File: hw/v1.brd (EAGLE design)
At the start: 32 x 37 mm, 43 parts, among them J1 FFC2B28-24-G, J2 S2B-PH-SM4-TB(LF)(SN), J3 10118193-0001LF, Q1 SI1308EDL-T1-GE3, SW1 SMD-BUTTON(4P-5.2X5.2X1.5MM-S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, U1 ESP32-C3-WROOM-02-H4, U2 PCF85063ATT/AJ, U3 TLV1117LV33DCYR

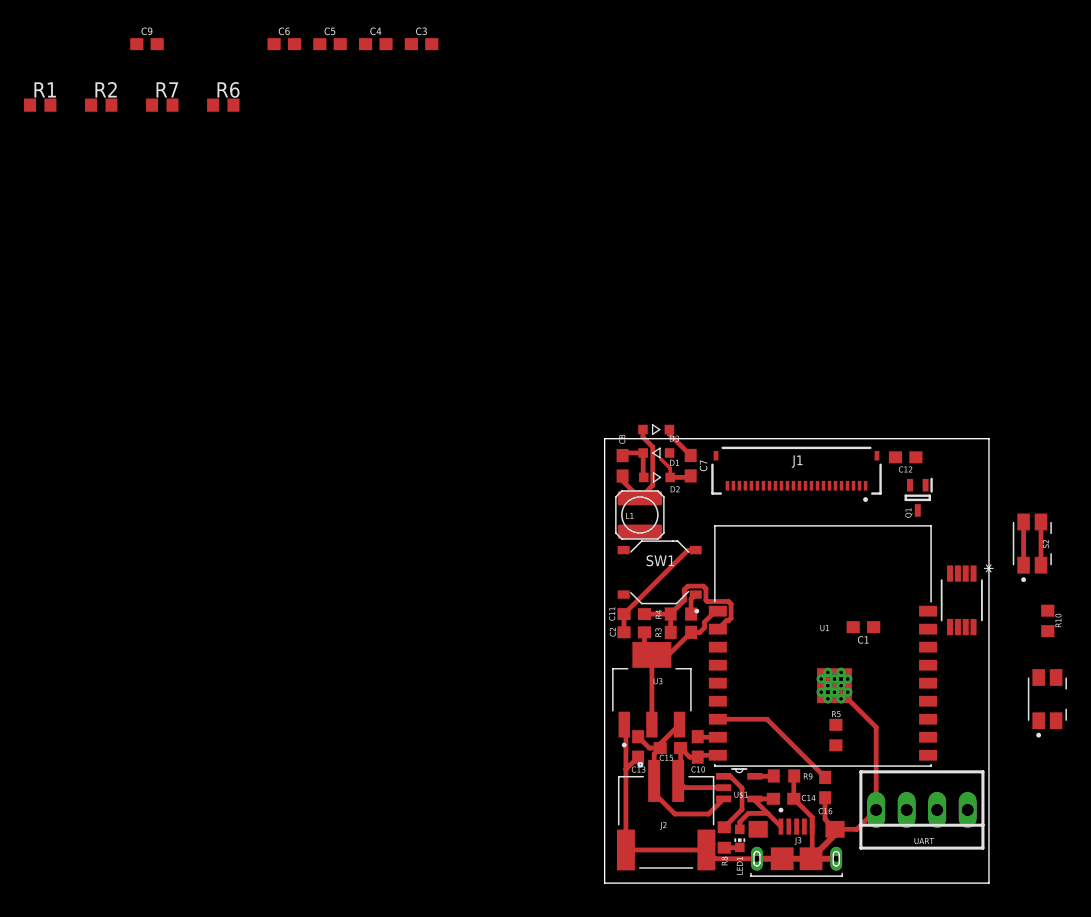
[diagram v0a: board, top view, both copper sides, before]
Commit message: Finish basic board layout, change reset button
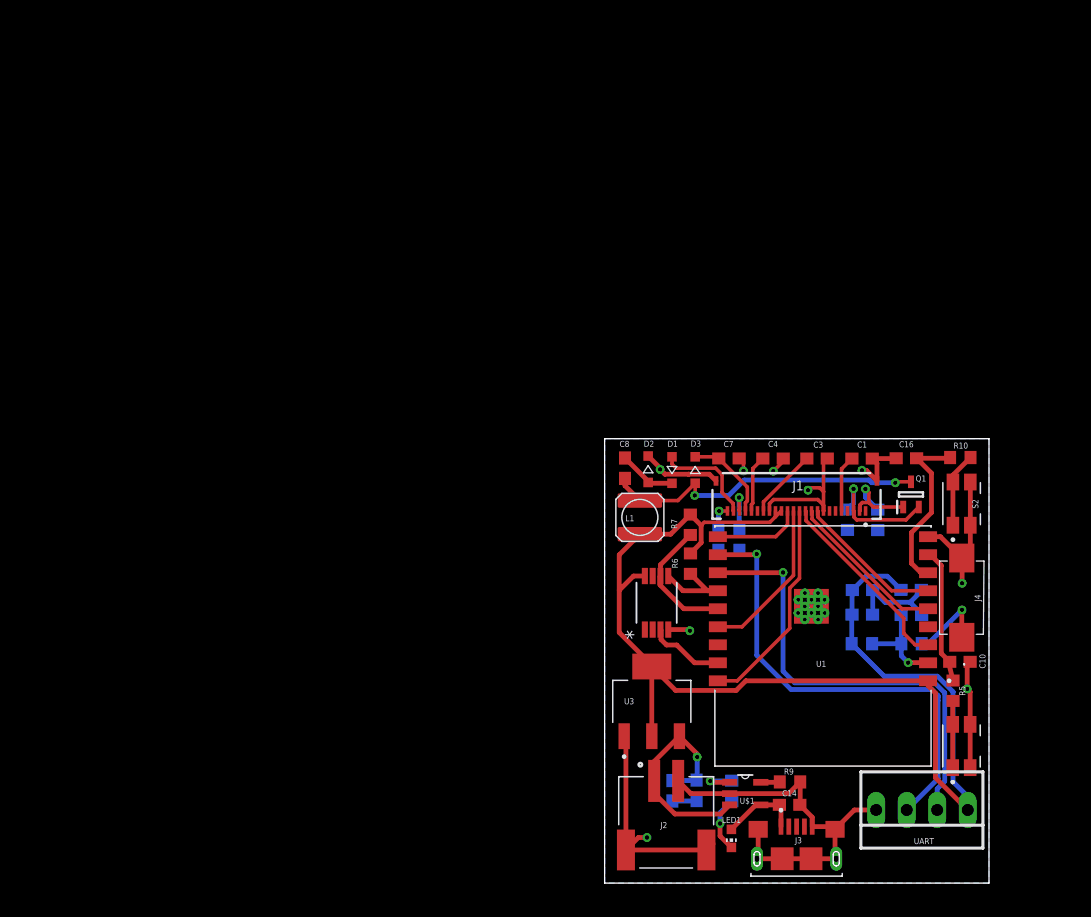
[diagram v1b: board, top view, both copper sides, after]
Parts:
- removed SW1: SMD-BUTTON(4P-5.2X5.2X1.5MM-SKQGADE010)-SKQGADE010, SMD-BUTTON_4P-5.2X5.2X1.5MM-SKQGADE010_:SW4-SMD-5.2X5.2X1.5MM
- added J4: PTS636_SM25F_SMTR_LFS, PTS636_SM25F_SMTR_LFS:PTS636SM25FSMTRLFS
- moved C9 78.2 mm to (25.5, 24.4), flipped to the bottom, turned to 180 degrees
- moved R1 77.8 mm to (22.7, 30.2), flipped to the bottom, turned to 90 degrees
- moved R2 71.1 mm to (20.2, 30.3), flipped to the bottom, turned to 90 degrees
- moved R7 56.2 mm to (7.13, 29.8), turned to 90 degrees
- moved C6 54.9 mm to (9.48, 28.6), flipped to the bottom, turned to 270 degrees
- moved R6 54.5 mm to (7.15, 26.6), turned to 90 degrees
- moved C5 53.5 mm to (11.2, 28.6), flipped to the bottom, turned to 270 degrees
- moved C4 47.8 mm to (14.0, 35.4)
- moved C3 47.7 mm to (17.7, 35.3)
- moved C16 28.2 mm to (25.1, 35.4), turned to 180 degrees
- moved U2 25.4 mm to (4.33, 23.3), turned to 90 degrees
- moved C11 23.1 mm to (25.5, 22.3), flipped to the bottom
- moved C10 23.0 mm to (29.6, 18.4), turned to 0 degrees
- moved R4 19.4 mm to (25.6, 19.9), flipped to the bottom, turned to 0 degrees
- moved C2 19.0 mm to (21.5, 22.3), flipped to the bottom
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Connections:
- net BUSY: now also U1.6; no longer U1.3
- net CS: now also U1.18; no longer U1.10
- net D/C: now also U1.3; no longer U1.15
- net GND: now also J4.2; no longer SW1.3
- net MOSI: now also U1.10; no longer U1.6
- net N$8: now also J4.1; no longer SW1.1
- net RES: now also U1.5; no longer U1.18
- net SCK: now also U1.15; no longer U1.5
- net SCL: now also R7.1, U1.14; no longer R6.1, U1.13
- net SDA: now also R6.1, U1.13; no longer R7.1, U1.14
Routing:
- net 3V3: track 15.4 -> 104.0 mm
- net N$12: track 0.00 -> 38.8 mm, vias 0 -> 1
- net GND: track 89.8 -> 127.8 mm, vias 0 -> 9
- net N$11: track 0.00 -> 37.9 mm, vias 0 -> 1
- net N$5: track 8.94 -> 27.3 mm, vias 0 -> 2
- net CS: track 0.00 -> 17.9 mm
- net D/C: track 0.00 -> 16.0 mm
- net RES: track 0.00 -> 13.4 mm
- net SCK: track 0.00 -> 13.4 mm
- net BUSY: track 0.00 -> 12.2 mm
- net SCL: track 0.00 -> 10.8 mm
- net RESE: track 0.00 -> 10.2 mm, vias 0 -> 1
- net BTN2: track 2.20 -> 11.4 mm
- net PREVGL: track 0.00 -> 8.55 mm
- net GDR: track 0.00 -> 7.76 mm, vias 0 -> 1
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- added copper zone on layer 16, net GND
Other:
- board text added: "Ian Feldman 2024"

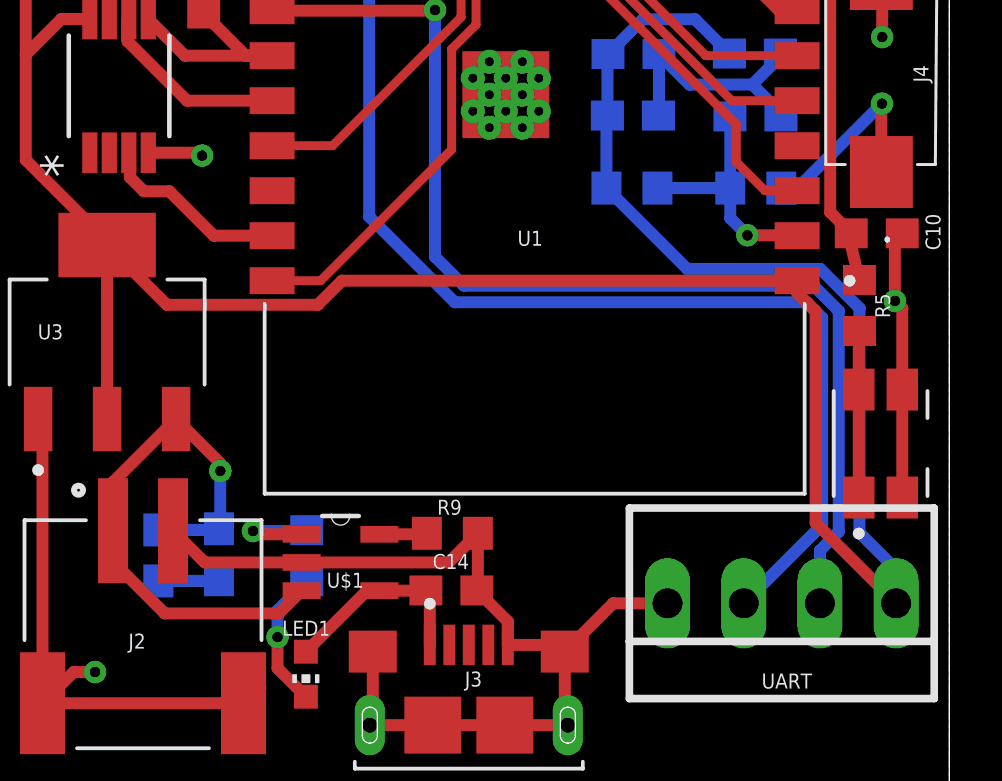
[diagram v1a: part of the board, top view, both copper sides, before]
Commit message: Add temperature sensor
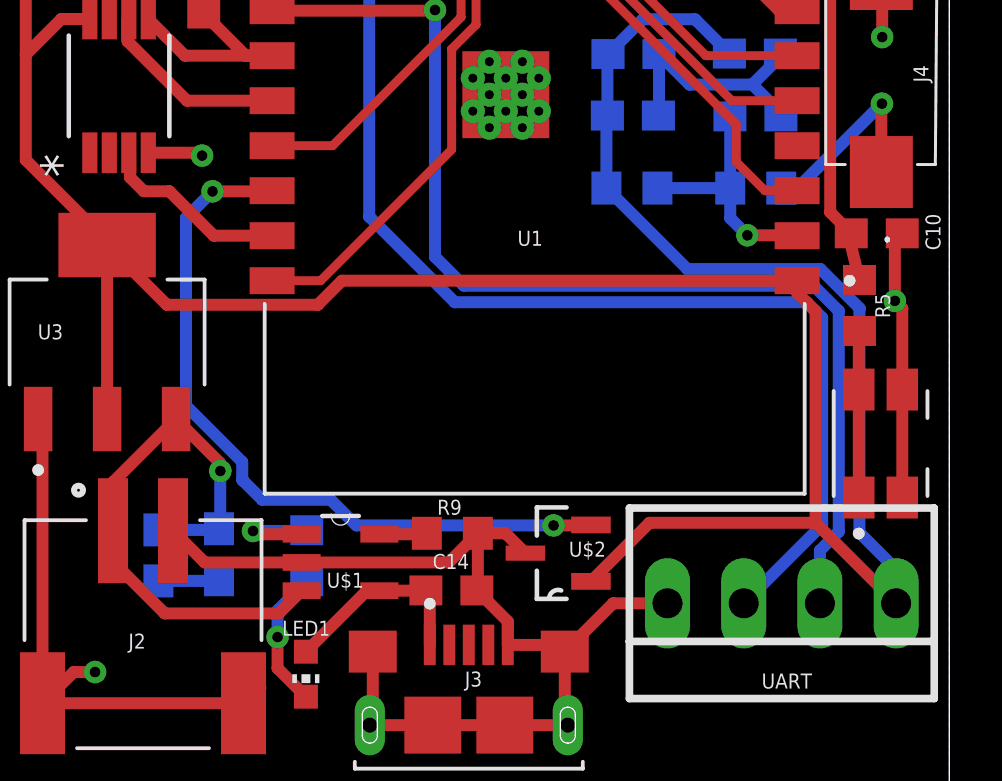
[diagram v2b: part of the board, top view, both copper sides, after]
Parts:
- added U$2: MCP9700T-E/TT, MCP9700T-E_TT:SOT95P237X112-3N
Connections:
- new net TEMP: U$2.2, U1.16
- net 3V3: now also U$2.1
- net GND: now also U$2.3
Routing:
- net TEMP: track 0.00 -> 25.0 mm, vias 0 -> 2
- net 3V3: track 104.0 -> 112.3 mm
- net GND: track 127.8 -> 129.7 mm
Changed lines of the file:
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@@
 <attribute name="VALUE" x="29.734175" y="23.215065625" size="1.27" layer="27" rot="R90" align="center"/>
+</element>
+<element name="U$2" library="MCP9700T-E_TT" package="SOT95P237X112-3N" value="MCP9700T-E/TT" x="18.962759375" y="7.76104375" smashed="yes" rot="R180">
+<attribute name="AVAILABILITY" value="In Stock" x="18.962759375" y="7.76104375" size="1.778" layer="27" rot="R180" display="off"/>
+<attribute name="CHECK_PRICES" value="https://www.snapeda.com/parts/MCP9700T-E/TT/Microchip/view-part/?ref=eda" x="18.962759375" y="7.76104375" size="1.778" layer="27" rot="R180" display="off"/>
+<attribute name="DESCRIPTION" value=" Microchip MCP9700T-E/TT Temperature Sensor 3-Pin SOT-23, -40 - +125 degC | Microchip Technology Inc. MCP9700T-E/TT " x="18.962759375" y="7.76104375" size="1.778" layer="27" rot="R180" display="off"/>
+<attribute name="MF" value="Microchip" x="18.962759375" y="7.76104375" size="1.778" layer="27" rot="R180" display="off"/>
+<attribute name="MP" value="MCP9700T-E/TT" x="18.962759375" y="7.76104375" size="1.778" layer="27" rot="R180" display="off"/>
+<attribute name="NAME" x="19.31835625" y="7.64379375" size="0.5" layer="25" ratio="10" rot="SR0"/>
+<attribute name="PACKAGE" value="SOT-23-3 Microchip" x="18.962759375" y="7.76104375" size="1.778" layer="27" rot="R180" display="off"/>
+<attribute name="PRICE" value="None" x="18.962759375" y="7.76104375" size="1.778" layer="27" rot="R180" display="off"/>
+<attribute name="PURCHASE-URL" value="https://www.snapeda.com/api/url_track_click_mouser/?unipart_id=134539&amp;manufacturer=Microchip&amp;part_name=MCP9700T-E/TT&amp;search_term=None" x="18.962759375" y="7.76104375" size="1.778" layer="27" rot="R180" display="off"/>
+<attribute name="SNAPEDA_LINK" value="https://www.snapeda.com/parts/MCP9700T-E/TT/Microchip/view-part/?ref=snap" x="18.962759375" y="7.76104375" size="1.778" layer="27" rot="R180" display="off"/>
+<attribute name="VALUE" x="45.554859375" y="41.97814375" size="16.0336" layer="27" ratio="10" rot="SR180"/>
 </element>
 </elements>
@@
 <wire x1="29.002090625" y1="8.443578125" x2="29.002090625" y2="15.914084375" width="0.4" layer="16"/>
 <wire x1="29.002090625" y1="15.914084375" x2="29.01116875" y2="15.9231625" width="0.4" layer="16"/>
+<contactref element="U$2" pad="1"/>
+<wire x1="20.054959375" y1="6.82124375" x2="22.006821875" y2="8.77310625" width="0.4" layer="1"/>
+<wire x1="22.006821875" y1="8.77310625" x2="27.542853125" y2="8.77310625" width="0.4" layer="1"/>
 </signal>
 <signal name="N$3">
@@
 <wire x1="19.183621875" y1="4.028103125" x2="19.183621875" y2="4.478103125" width="0.5" layer="1"/>
 <wire x1="18.958621875" y1="4.703103125" x2="19.183621875" y2="4.478103125" width="0.5" layer="1"/>
-<wire x1="16.28484375" y1="8.422190625" x2="16.2516" y2="8.388946875" width="0.4" layer="1"/>
+<wire x1="16.2516" y1="8.388946875" x2="16.28484375" y2="8.422190625" width="0.4" layer="1"/>
 <wire x1="17.283621875" y1="2.128103125" x2="17.183621875" y2="2.028103125" width="0.4" layer="1"/>
 <wire x1="30.447690625" y1="33.394334375" x2="30.447690625" y2="29.794334375" width="0.4" layer="1"/>
@@
 <wire x1="18.225078125" y1="32.590196875" x2="18.225078125" y2="30.983421875" width="0.3" layer="1"/>
 <wire x1="18.225078125" y1="30.983421875" x2="18.22508125" y2="30.98341875" width="0.3" layer="1"/>
+<contactref element="U$2" pad="3"/>
+<wire x1="16.28484375" y1="8.422190625" x2="17.2094125" y2="8.422190625" width="0.4" layer="1"/>
+<wire x1="17.2094125" y1="8.422190625" x2="17.870559375" y2="7.76104375" width="0.4" layer="1"/>
 </signal>
 <signal name="N$7">
@@
 <wire x1="26.938940625" y1="19.92760625" x2="29.753978125" y2="22.74264375" width="0.4" layer="16"/>
 </signal>
+<signal name="TEMP">
+<contactref element="U$2" pad="2"/>
+<via x="7.440103125" y="19.821165625" extent="1-16" drill="0.35"/>
+<via x="18.80869375" y="8.68548125" extent="1-16" drill="0.35"/>
+<contactref element="U1" pad="16"/>
+<wire x1="20.054959375" y1="8.70084375" x2="20.039596875" y2="8.68548125" width="0.4" layer="1"/>
+<wire x1="20.039596875" y1="8.68548125" x2="18.80869375" y2="8.68548125" width="0.4" layer="1"/>
+<wire x1="7.440103125" y1="19.821165625" x2="9.4055" y2="19.821165625" width="0.4" layer="1"/>
+<wire x1="9.4055" y1="19.821165625" x2="9.427359375" y2="19.843025" width="0.4" layer="1"/>
+<wire x1="18.80869375" y1="8.68548125" x2="12.235609375" y2="8.68548125" width="0.4" layer="16"/>
+<wire x1="11.378065625" y1="9.543025" x2="9.09451875" y2="9.543025" width="0.4" layer="16"/>
+<wire x1="8.460940625" y1="10.176603125" x2="8.460665625" y2="10.176603125" width="0.4" layer="16"/>
+<wire x1="9.09451875" y1="9.543025" x2="8.460940625" y2="10.176603125" width="0.4" layer="16"/>
+<wire x1="8.460665625" y1="10.176603125" x2="8.4306" y2="10.20666875" width="0.4" layer="16"/>
+<wire x1="8.4306" y1="10.20666875" x2="8.4306" y2="10.802625" width="0.4" layer="16"/>
+<wire x1="8.4306" y1="10.802625" x2="6.556509375" y2="12.676715625" width="0.4" layer="16"/>
+<wire x1="6.556509375" y1="18.937571875" x2="7.440103125" y2="19.821165625" width="0.4" layer="16"/>
+<wire x1="12.235609375" y1="8.68548125" x2="11.378065625" y2="9.543025" width="0.4" layer="16"/>
+<wire x1="6.556509375" y1="12.676715625" x2="6.556509375" y2="18.937571875" width="0.4" layer="16"/>
+</signal>
 </signals>

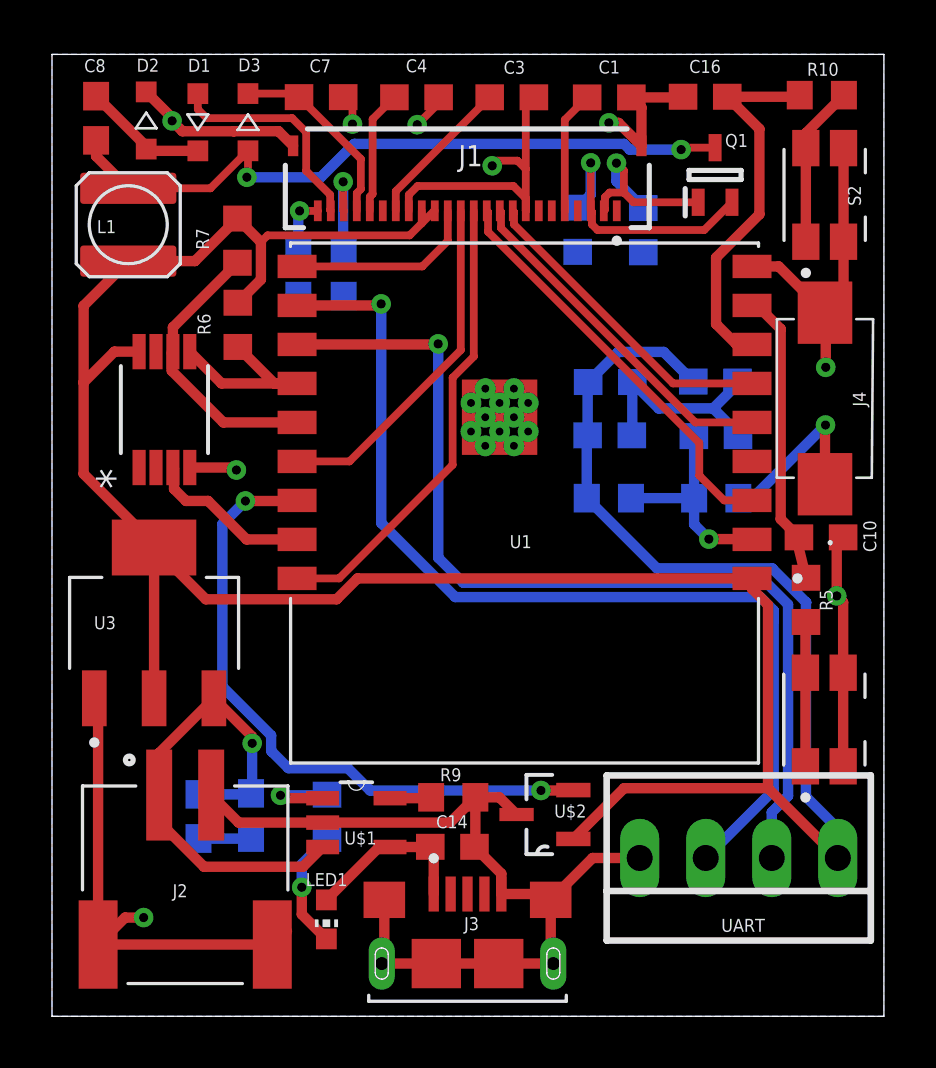
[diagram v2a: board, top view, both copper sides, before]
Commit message: Change inductor, add part numbers to bom
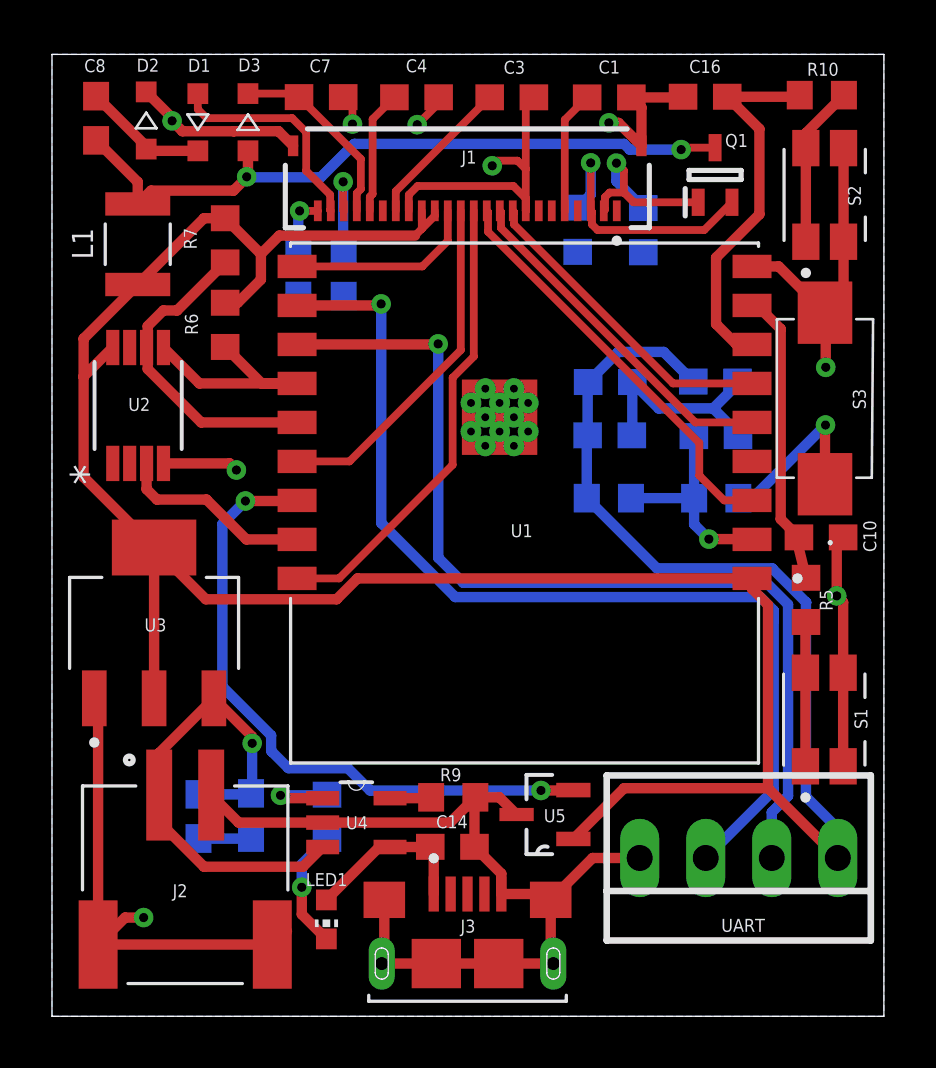
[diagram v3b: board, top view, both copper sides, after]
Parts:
- L1: value (none) -> 47 uH; device we-power:L_NR40XX -> ADL3225V-470MT-TL000:IND_ADL3225V-470MT-TL000
- moved U2 1.02 mm to (3.31, 23.5)
- moved L1 0.83 mm to (3.30, 29.7), turned to 90 degrees
- moved R6 0.49 mm to (6.66, 26.6)
- moved R7 0.47 mm to (6.66, 29.8)
- renumbered J4 to S3, U$1 to U4, U$2 to U5
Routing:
- net SDA: track 7.49 -> 9.06 mm
- net SCL: track 10.8 -> 12.3 mm
- net RTC_INT: track 6.38 -> 7.58 mm
- net 3V3: track 112.3 -> 111.3 mm
- net GND: track 129.7 -> 130.6 mm
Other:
- board text added: "S1"
- board text added: "U2"

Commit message: Find passive parts, change led resistor to 300 ohm
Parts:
- R8: value 470 -> 300
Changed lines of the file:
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@@
 <attribute name="VALUE" x="8.566240625" y="29.212334375" size="1.27" layer="27" rot="R90"/>
 </element>
-<element name="R8" library="rcl" library_urn="urn:adsk.eagle:library:334" package="R0603" package3d_urn="urn:adsk.eagle:package:23555/3" value="470" x="10.58005625" y="7.67623125" smashed="yes" rot="MR270">
+<element name="R8" library="rcl" library_urn="urn:adsk.eagle:library:334" package="R0603" package3d_urn="urn:adsk.eagle:package:23555/3" value="300" x="10.58005625" y="7.67623125" smashed="yes" rot="MR270">
 <attribute name="NAME" x="10.186375" y="6.0475875" size="0.5" layer="26" rot="MR180"/>
 <attribute name="POPULARITY" value="77" x="75.35005625" y="-13.91376875" size="1.778" layer="28" rot="MR270" display="off"/>

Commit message: Hw changes
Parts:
- removed UART: 22-23-2041, con-molex:22-23-2041
- added J4: 851-43-004-20-001000, 851-43-004-20-001000:CONN_851-43-004-20-001000_MIM
- added LED2: (no value), led:CHIP-LED0603
- added R11: 120, rcl:R0603
- added R12: 100k, rcl:R0603
- moved U5 0.59 mm to (19.6, 7.75)
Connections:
- new net DEBUG: R11.2, U1.4
- new net N$17: LED2.A, R11.1
- net 3V3: now also J4.4, R12.2; no longer UART.1
- net GND: now also J4.1, LED2.C; no longer UART.4
- net N$11: now also J4.3; no longer UART.2
- net N$12: now also J4.2; no longer UART.3
- net TEMP: now also R12.1
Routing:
- net DEBUG: track 0.00 -> 13.2 mm, vias 0 -> 1
- net TEMP: track 25.0 -> 28.2 mm
- net N$17: track 0.00 -> 2.48 mm
- net D/C: track 16.0 -> 18.0 mm
- net N$11: track 37.9 -> 39.6 mm
- net GND: track 130.6 -> 132.2 mm
- net 3V3: track 111.3 -> 112.8 mm
- net N$12: track 38.8 -> 40.0 mm
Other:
- board text added: "3V3"
- board text added: "GND"
- board text added: "RX"
- board text added: "TX"
